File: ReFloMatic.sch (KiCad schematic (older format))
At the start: 39 parts, among them CON1 BARREL_JACK, CON2 MicroSD_Card, P1 PROG, P2 THERMOCOUPLE, P3 DOOR_SERVO, P4 OVEN, Q1 MMUN2211, Q2 MMUN2111, Q3 MMUN2111, Q4 MMUN2211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

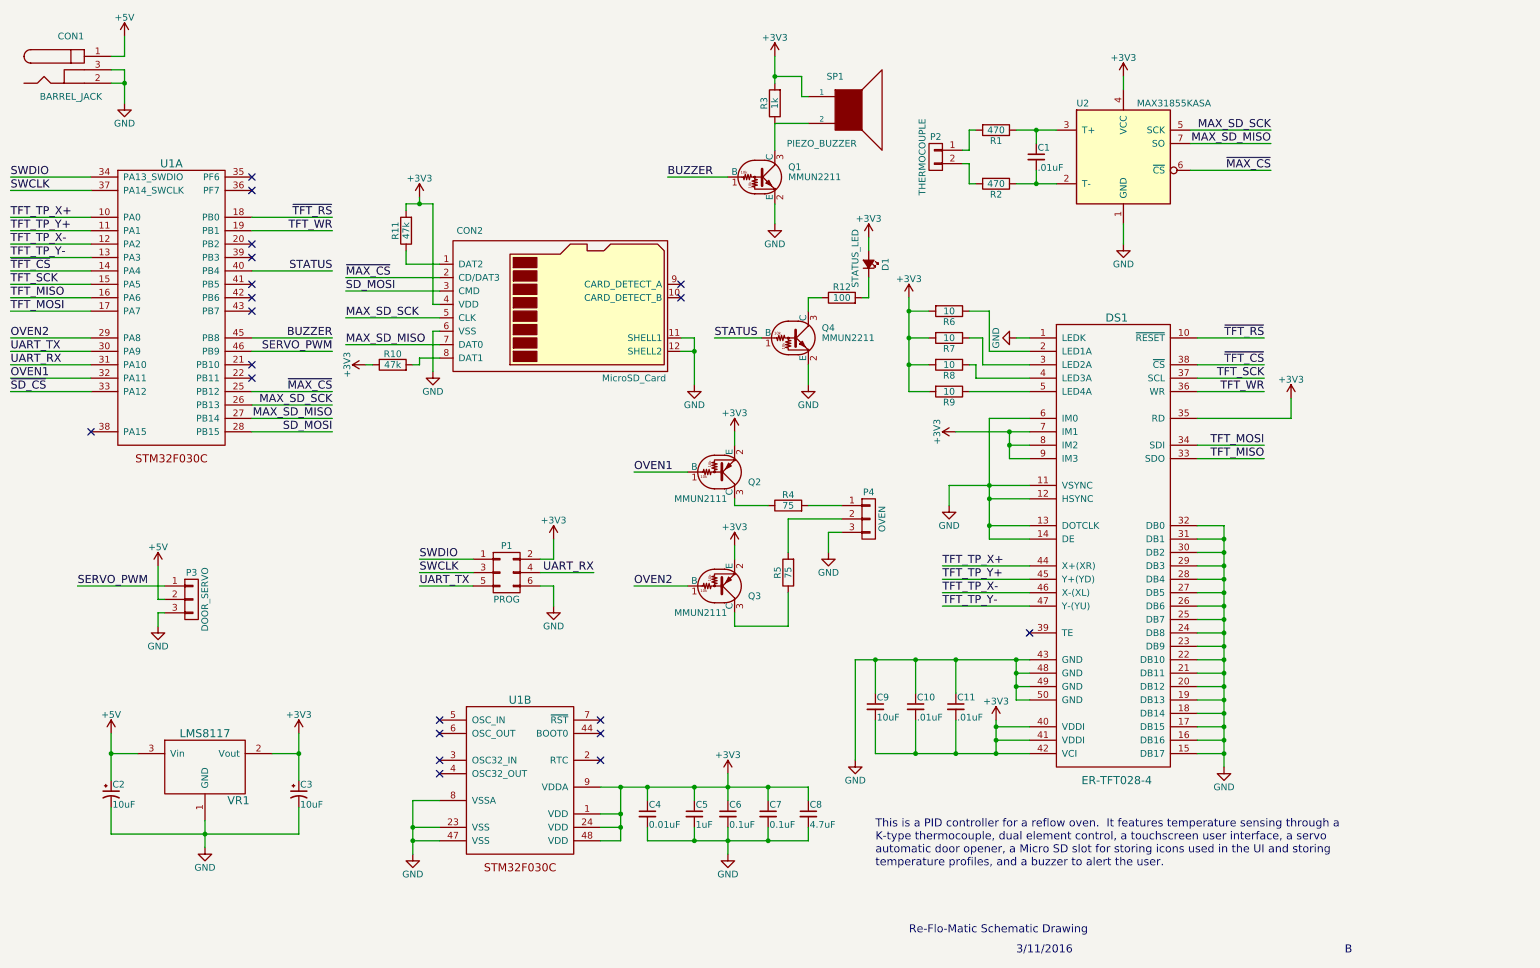
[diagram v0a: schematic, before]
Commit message: Finished associating all parts and creating all footprints and 3D models.  Minor changes to schematic.  Started layout.
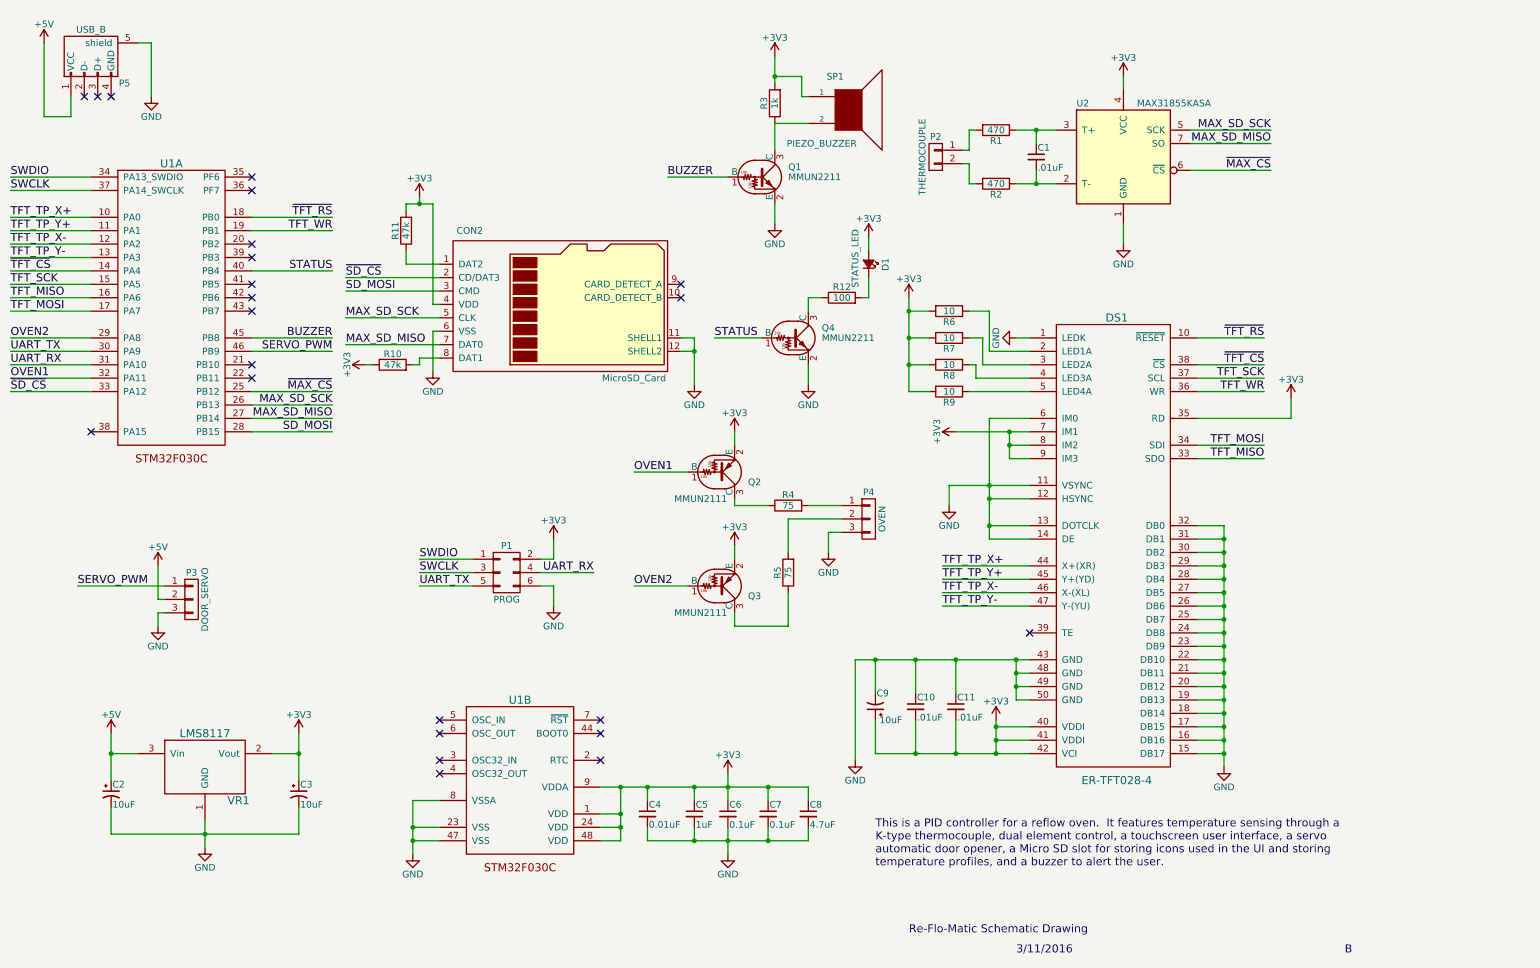
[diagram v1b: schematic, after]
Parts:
- removed C9: 10uF, symbol C_Small
- removed CON1: BARREL_JACK, Barrel_Jacks:CONN-POWER-JACK-SMD-2.1X5.5MM, symbol BARREL_JACK
- added C9: 10uF, SMD_Packages:SMD-1206_Pol, symbol CP1_Small
- added P5: USB_B, Connectors-Custom3:SMT-Micro-USB-AB, symbol USB_B
- C2, C3: footprint (none) -> SMD_Packages:SMD-1206_Pol
- C8: footprint (none) -> Capacitors_SMD:C_0805
- P1: footprint (none) -> Connectors-Custom3:HEADER_2X3_SMD
- P2: footprint (none) -> Connectors-Custom:TERMINAL-BLOCK-3.5MM-2POS
- P3: footprint (none) -> Connectors-Custom3:HEADER_1X3_SMD
- P4: footprint (none) -> Connectors-Custom:TERMINAL-BLOCK-3.5MM-3POS
- SP1: footprint (none) -> Speaker:PS1240P02BT
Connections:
- net +3V3: now also C9.1
- net +5V: now also P5.1 (VCC)
- net GND: now also C9.2, P5.5 (shield)
- net ~MAX_CS: no longer CON2.2 (CD/DAT3)
- net ~SD_CS: now also CON2.2 (CD/DAT3)
- no-connect marks 20 -> 23

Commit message: Added TFT footprint that contains display and PCB cutout.
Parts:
- DS1: footprint TFT:FPC_50 -> TFT:ER-TFT028-4
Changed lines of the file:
@@
 F 0 "DS1" H 8900 6300 60  0000 C CNN
 F 1 "ER-TFT028-4" H 8900 2850 60  0000 C CNN
-F 2 "TFT:FPC_50" H 8850 6300 60  0001 C CNN
+F 2 "TFT:ER-TFT028-4" H 8850 6300 60  0001 C CNN
 F 3 "" H 8850 6300 60  0000 C CNN
 	1    8900 4600

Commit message: Preliminary component placement.
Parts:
- added P6: PWR_CONN, Pin_Headers:Pin_Header_Straight_1x02, symbol CONN_01X02
- P3: footprint Connectors-Custom3:HEADER_1X3_SMD -> Pin_Headers:Pin_Header_Straight_1x03
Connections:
- net +5V: now also P6.1 (P1)
- net GND: now also P6.2 (P2)
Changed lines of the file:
@@
 F 0 "P3" H 2000 5200 50  0000 C CNN
 F 1 "DOOR_SERVO" V 2100 5000 50  0000 C CNN
-F 2 "Connectors-Custom3:HEADER_1X3_SMD" H 2000 5000 50  0001 C CNN
+F 2 "Pin_Headers:Pin_Header_Straight_1x03" H 2000 5000 50  0001 C CNN
 F 3 "" H 2000 5000 50  0000 C CNN
 	1    2000 5000
@@
 NoConn ~ 1300 1250
 NoConn ~ 1400 1250
+$Comp
+L CONN_01X02 P6
+U 1 1 56E5E1F2
+P 2400 1050
+F 0 "P6" H 2400 1200 50  0000 C CNN
+F 1 "PWR_CONN" V 2500 1050 50  0000 C CNN
+F 2 "Pin_Headers:Pin_Header_Straight_1x02" H 2400 1050 50  0001 C CNN
+F 3 "" H 2400 1050 50  0000 C CNN
+	1    2400 1050
+	1    0    0    -1
+$EndComp
+$Comp
+L +5V #PWR034
+U 1 1 56E5E38F
+P 2100 900
+F 0 "#PWR034" H 2100 750 50  0001 C CNN
+F 1 "+5V" H 2100 1040 50  0000 C CNN
+F 2 "" H 2100 900 50  0000 C CNN
+F 3 "" H 2100 900 50  0000 C CNN
+	1    2100 900
+	1    0    0    -1
+$EndComp
+$Comp
+L GND #PWR035
+U 1 1 56E5E415
+P 2100 1200
+F 0 "#PWR035" H 2100 950 50  0001 C CNN
+F 1 "GND" H 2100 1050 50  0000 C CNN
+F 2 "" H 2100 1200 50  0000 C CNN
+F 3 "" H 2100 1200 50  0000 C CNN
+	1    2100 1200
+	1    0    0    -1
+$EndComp
+Wire Wire Line
+	2200 1100 2100 1100
+Wire Wire Line
+	2100 1100 2100 1200
+Wire Wire Line
+	2200 1000 2100 1000
+Wire Wire Line
+	2100 1000 2100 900
 $EndSCHEMATC
